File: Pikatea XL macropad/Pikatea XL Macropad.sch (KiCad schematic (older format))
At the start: 40 parts, among them J1 TC2030-CTX, J2 USB_B_Mini, J3 Conn_01x03_Male, J7 Conn_01x03_Male, SW1 SW_DPST, SW2 Rotary_Encoder_Switch, SW3 Rotary_Encoder_Switch, U1 ATMEGA32U4-EP, X1 16MHz

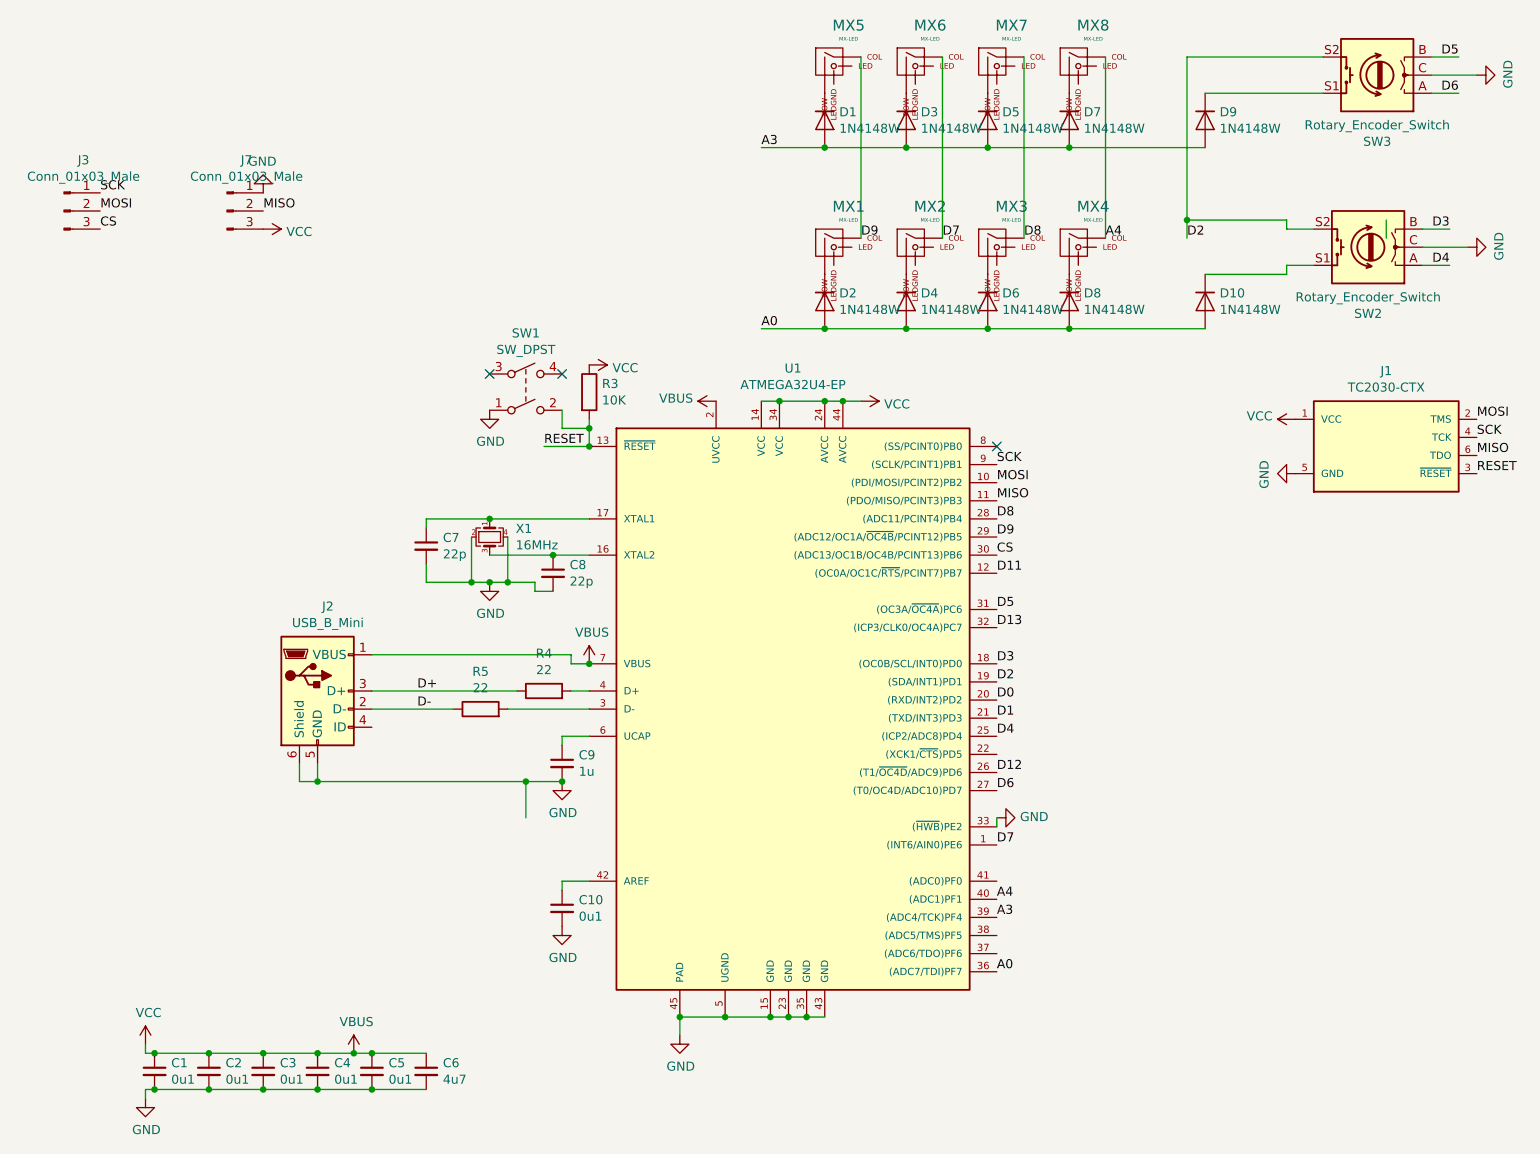
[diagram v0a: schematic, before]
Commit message: add xl macropad pcb
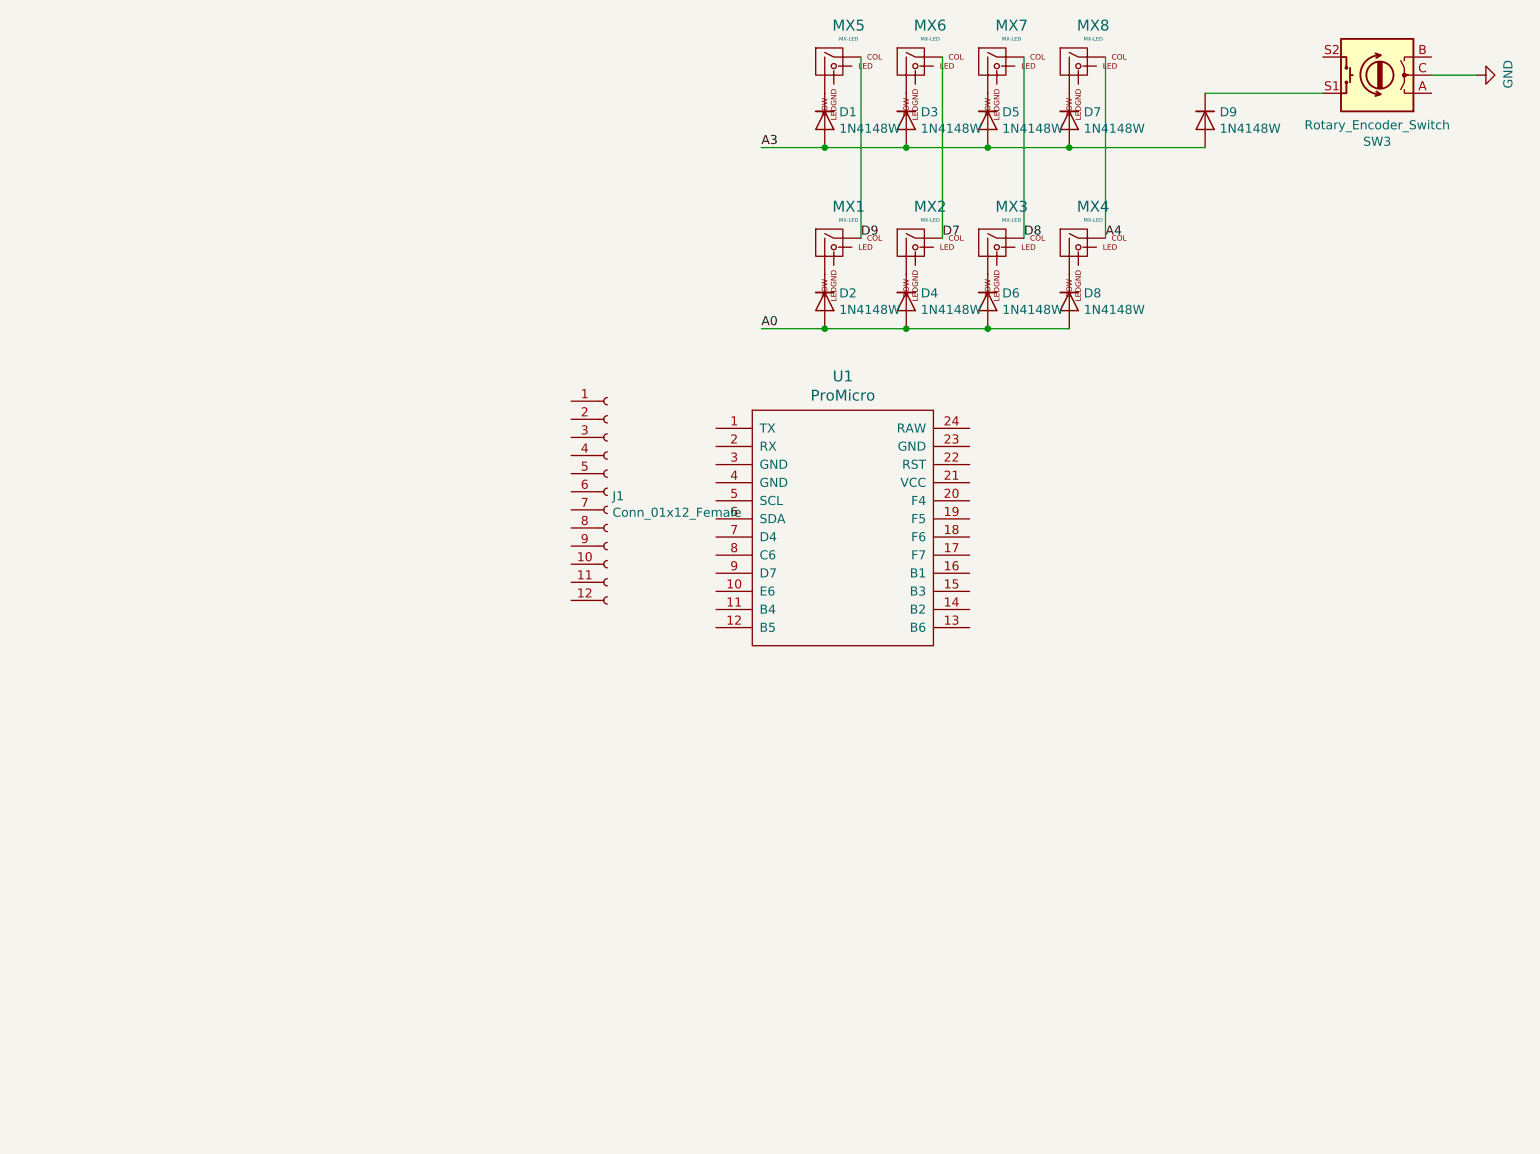
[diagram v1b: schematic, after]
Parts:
- removed C1, C10, C2, C3, C4, C5: 0u1, Capacitor_SMD:C_0805_2012Metric, symbol Device:C_Small
- removed C6: 4u7, Capacitor_SMD:C_0805_2012Metric, symbol Device:C_Small
- removed C7, C8: 22p, Capacitor_SMD:C_0805_2012Metric, symbol Device:C_Small
- removed C9: 1u, Capacitor_SMD:C_0805_2012Metric, symbol Device:C_Small
- removed D10: 1N4148W, Diode_SMD:D_SOD-123, symbol Diode:1N4148W
- removed J1: TC2030-CTX, TC2030-CTX:TC2030-IDC, symbol TC2030-CTX:TC2030-CTX
- removed J2: USB_B_Mini, usb_mini:USB-Mini-B_ LCSC-C46398, symbol Connector:USB_B_Mini
- removed J3, J7: Conn_01x03_Male, Connector_PinHeader_2.54mm:PinHeader_1x03_P2.54mm_Vertical, symbol Connector:Conn_01x03_Male
- removed R3: 10K, Resistor_SMD:R_0805_2012Metric, symbol Device:R
- removed R4, R5: 22, Resistor_SMD:R_0805_2012Metric, symbol Device:R
- removed SW1: SW_DPST, Button_Switch_SMD:SW_SPST_TL3342, symbol Switch:SW_DPST
- removed SW2: Rotary_Encoder_Switch, Pikatea Macropad Encoder Side Mount:Encoder-BI_EN11_HSM0E, symbol Device:Rotary_Encoder_Switch
- removed U1: ATMEGA32U4-EP, Package_QFP:LQFP-44_10x10mm_P0.8mm, symbol atmega32u4-ep:ATMEGA32U4-EP
- removed X1: 16MHz, Crystal:Crystal_SMD_SeikoEpson_FA238-4Pin_3.2x2.5mm, symbol Device:Crystal_GND24_Small
- added J1: Conn_01x12_Female, Connector_PinHeader_2.54mm:PinHeader_1x12_P2.54mm_Vertical, symbol Connector:Conn_01x12_Female
- added U1: ProMicro, promicro:ProMicro, symbol promicro:ProMicro
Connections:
- net labels removed: CS, D+, D-, D0, D1, D11, D12, D13, D2, D3, D4, D5, D6, MISO, MOSI, RESET, SCK, VBUS, VCC
- wire segments 93 -> 15
- no-connect marks 3 -> 0

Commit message: updates to XL macropad
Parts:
- D1, D2, D3, D4, D5, D6, D7, D8, D9: footprint Diode_SMD:D_SOD-123 -> keyboard_parts:D_axial
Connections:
- net A0: now also J1.11 (Pin_11), U1.11 (B4)
- net A3: now also J1.10 (Pin_10), U1.10 (E6)
- net A4: now also J1.12 (Pin_12), U1.12 (B5)
- net D7: now also J1.8 (Pin_8), U1.8 (C6)
- net D9: now also J1.9 (Pin_9), U1.9 (D7)
- net GND: now also J1.3 (Pin_3), J1.4 (Pin_4), U1.3 (GND), U1.4 (GND)
- net A: now reaches SW3.A
- net A: now also J1.7 (Pin_7), U1.7 (D4)
- net B: now reaches SW3.B
- net B: now also J1.6 (Pin_6), U1.6 (SDA)
- net A10: now reaches SW3.S2
- net A10: now also J1.1 (Pin_1), U1.1 (TX)
- net at J1.2 (Pin_2): now also U1.2 (RX)
- net at J1.5 (Pin_5): now also U1.5 (SCL)
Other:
- moved on the sheet: J1
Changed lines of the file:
@@
 F 0 "D1" V 7204 1330 50  0000 L CNN
 F 1 "1N4148W" V 7295 1330 50  0000 L CNN
-F 2 "Diode_SMD:D_SOD-123" H 7250 1075 50  0001 C CNN
+F 2 "keyboard_parts:D_axial" H 7250 1075 50  0001 C CNN
 F 3 "https://www.vishay.com/docs/85748/1n4148w.pdf" H 7250 1250 50  0001 C CNN
 	1    7250 1250
@@
 F 0 "D3" V 7654 1330 50  0000 L CNN
 F 1 "1N4148W" V 7745 1330 50  0000 L CNN
-F 2 "Diode_SMD:D_SOD-123" H 7700 1075 50  0001 C CNN
+F 2 "keyboard_parts:D_axial" H 7700 1075 50  0001 C CNN
 F 3 "https://www.vishay.com/docs/85748/1n4148w.pdf" H 7700 1250 50  0001 C CNN
 	1    7700 1250
@@
 F 0 "D5" V 8104 1330 50  0000 L CNN
 F 1 "1N4148W" V 8195 1330 50  0000 L CNN
-F 2 "Diode_SMD:D_SOD-123" H 8150 1075 50  0001 C CNN
+F 2 "keyboard_parts:D_axial" H 8150 1075 50  0001 C CNN
 F 3 "https://www.vishay.com/docs/85748/1n4148w.pdf" H 8150 1250 50  0001 C CNN
 	1    8150 1250
@@
 F 0 "D7" V 8554 1330 50  0000 L CNN
 F 1 "1N4148W" V 8645 1330 50  0000 L CNN
-F 2 "Diode_SMD:D_SOD-123" H 8600 1075 50  0001 C CNN
+F 2 "keyboard_parts:D_axial" H 8600 1075 50  0001 C CNN
 F 3 "https://www.vishay.com/docs/85748/1n4148w.pdf" H 8600 1250 50  0001 C CNN
 	1    8600 1250
@@
 F 0 "D9" V 9304 1330 50  0000 L CNN
 F 1 "1N4148W" V 9395 1330 50  0000 L CNN
-F 2 "Diode_SMD:D_SOD-123" H 9350 1075 50  0001 C CNN
+F 2 "keyboard_parts:D_axial" H 9350 1075 50  0001 C CNN
 F 3 "https://www.vishay.com/docs/85748/1n4148w.pdf" H 9350 1250 50  0001 C CNN
 	1    9350 1250
@@
 F 0 "D2" V 7204 2330 50  0000 L CNN
 F 1 "1N4148W" V 7295 2330 50  0000 L CNN
-F 2 "Diode_SMD:D_SOD-123" H 7250 2075 50  0001 C CNN
+F 2 "keyboard_parts:D_axial" H 7250 2075 50  0001 C CNN
 F 3 "https://www.vishay.com/docs/85748/1n4148w.pdf" H 7250 2250 50  0001 C CNN
 	1    7250 2250
@@
 F 0 "D4" V 7654 2330 50  0000 L CNN
 F 1 "1N4148W" V 7745 2330 50  0000 L CNN
-F 2 "Diode_SMD:D_SOD-123" H 7700 2075 50  0001 C CNN
+F 2 "keyboard_parts:D_axial" H 7700 2075 50  0001 C CNN
 F 3 "https://www.vishay.com/docs/85748/1n4148w.pdf" H 7700 2250 50  0001 C CNN
 	1    7700 2250
@@
 F 0 "D6" V 8104 2330 50  0000 L CNN
 F 1 "1N4148W" V 8195 2330 50  0000 L CNN
-F 2 "Diode_SMD:D_SOD-123" H 8150 2075 50  0001 C CNN
+F 2 "keyboard_parts:D_axial" H 8150 2075 50  0001 C CNN
 F 3 "https://www.vishay.com/docs/85748/1n4148w.pdf" H 8150 2250 50  0001 C CNN
 	1    8150 2250
@@
 F 0 "D8" V 8554 2330 50  0000 L CNN
 F 1 "1N4148W" V 8645 2330 50  0000 L CNN
-F 2 "Diode_SMD:D_SOD-123" H 8600 2075 50  0001 C CNN
+F 2 "keyboard_parts:D_axial" H 8600 2075 50  0001 C CNN
 F 3 "https://www.vishay.com/docs/85748/1n4148w.pdf" H 8600 2250 50  0001 C CNN
 	1    8600 2250
@@
 L Connector:Conn_01x12_Female J1
 U 1 1 61C5A4E4
-P 6050 3300
-F 0 "J1" H 6078 3276 50  0000 L CNN
-F 1 "Conn_01x12_Female" H 6078 3185 50  0000 L CNN
-F 2 "Connector_PinHeader_2.54mm:PinHeader_1x12_P2.54mm_Vertical" H 6050 3300 50  0001 C CNN
-F 3 "~" H 6050 3300 50  0001 C CNN
-	1    6050 3300
+P 6850 3450
+F 0 "J1" H 6878 3426 50  0000 L CNN
+F 1 "Conn_01x12_Female" H 6878 3335 50  0000 L CNN
+F 2 "Connector_PinHeader_2.54mm:PinHeader_1x12_P2.54mm_Vertical" H 6850 3450 50  0001 C CNN
+F 3 "~" H 6850 3450 50  0001 C CNN
+	1    6850 3450
 	1    0    0    -1
 $EndComp
@@
 	1    0    0    -1
 $EndComp
+Text Label 6650 4050 2    50   ~ 0
+A4
+Text Label 6650 3950 2    50   ~ 0
+A0
+Text Label 6650 3850 2    50   ~ 0
+A3
+Text Label 6650 3750 2    50   ~ 0
+D9
+Text Label 6650 3650 2    50   ~ 0
+D7
+Text Label 6650 3550 2    50   ~ 0
+A
+Text Label 6650 3450 2    50   ~ 0
+B
+Text Label 10600 1100 0    50   ~ 0
+A
+Text Label 10600 900  0    50   ~ 0
+B
+Text Label 10000 900  2    50   ~ 0
+A10
+Text Label 6650 2950 2    50   ~ 0
+A10
+$Comp
+L power:GND #PWR?
+U 1 1 61DC9E71
+P 6650 3250
+F 0 "#PWR?" H 6650 3000 50  0001 C CNN
+F 1 "GND" V 6655 3122 50  0000 R CNN
+F 2 "" H 6650 3250 50  0001 C CNN
+F 3 "" H 6650 3250 50  0001 C CNN
+	1    6650 3250
+	0    1    1    0
+$EndComp
+Connection ~ 6650 3250
+$Comp
+L power:GND #PWR?
+U 1 1 61DCA30D
+P 6650 3150
+F 0 "#PWR?" H 6650 2900 50  0001 C CNN
+F 1 "GND" V 6655 3022 50  0000 R CNN
+F 2 "" H 6650 3150 50  0001 C CNN
+F 3 "" H 6650 3150 50  0001 C CNN
+	1    6650 3150
+	0    1    1    0
+$EndComp
+Connection ~ 6650 3150
 $EndSCHEMATC

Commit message: update XL
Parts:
- MX1, MX2, MX3, MX4, MX5, MX6, MX7, MX8: footprint MX_Only:MXOnly-1U -> MX_Only:MXOnly-1U-NoLED
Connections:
- net D8: now also J1.5 (Pin_5), U1.5 (SCL)
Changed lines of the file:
@@
 F 0 "MX4" H 8732 2174 60  0000 C CNN
 F 1 "MX-LED" H 8732 2100 20  0000 C CNN
-F 2 "MX_Only:MXOnly-1U" H 8025 1925 60  0001 C CNN
+F 2 "MX_Only:MXOnly-1U-NoLED" H 8025 1925 60  0001 C CNN
 F 3 "" H 8025 1925 60  0001 C CNN
 	1    8650 1950
@@
 F 0 "MX3" H 8282 2174 60  0000 C CNN
 F 1 "MX-LED" H 8282 2100 20  0000 C CNN
-F 2 "MX_Only:MXOnly-1U" H 7575 1925 60  0001 C CNN
+F 2 "MX_Only:MXOnly-1U-NoLED" H 7575 1925 60  0001 C CNN
 F 3 "" H 7575 1925 60  0001 C CNN
 	1    8200 1950
@@
 F 0 "MX5" H 7382 1174 60  0000 C CNN
 F 1 "MX-LED" H 7382 1100 20  0000 C CNN
-F 2 "MX_Only:MXOnly-1U" H 6675 925 60  0001 C CNN
+F 2 "MX_Only:MXOnly-1U-NoLED" H 6675 925 60  0001 C CNN
 F 3 "" H 6675 925 60  0001 C CNN
 	1    7300 950
@@
 F 0 "MX6" H 7832 1174 60  0000 C CNN
 F 1 "MX-LED" H 7832 1100 20  0000 C CNN
-F 2 "MX_Only:MXOnly-1U" H 7125 925 60  0001 C CNN
+F 2 "MX_Only:MXOnly-1U-NoLED" H 7125 925 60  0001 C CNN
 F 3 "" H 7125 925 60  0001 C CNN
 	1    7750 950
@@
 F 0 "MX1" H 7382 2174 60  0000 C CNN
 F 1 "MX-LED" H 7382 2100 20  0000 C CNN
-F 2 "MX_Only:MXOnly-1U" H 6675 1925 60  0001 C CNN
+F 2 "MX_Only:MXOnly-1U-NoLED" H 6675 1925 60  0001 C CNN
 F 3 "" H 6675 1925 60  0001 C CNN
 	1    7300 1950
@@
 F 0 "MX2" H 7832 2174 60  0000 C CNN
 F 1 "MX-LED" H 7832 2100 20  0000 C CNN
-F 2 "MX_Only:MXOnly-1U" H 7125 1925 60  0001 C CNN
+F 2 "MX_Only:MXOnly-1U-NoLED" H 7125 1925 60  0001 C CNN
 F 3 "" H 7125 1925 60  0001 C CNN
 	1    7750 1950
@@
 F 0 "MX8" H 8732 1174 60  0000 C CNN
 F 1 "MX-LED" H 8732 1100 20  0000 C CNN
-F 2 "MX_Only:MXOnly-1U" H 8025 925 60  0001 C CNN
+F 2 "MX_Only:MXOnly-1U-NoLED" H 8025 925 60  0001 C CNN
 F 3 "" H 8025 925 60  0001 C CNN
 	1    8650 950
@@
 F 0 "MX7" H 8282 1174 60  0000 C CNN
 F 1 "MX-LED" H 8282 1100 20  0000 C CNN
-F 2 "MX_Only:MXOnly-1U" H 7575 925 60  0001 C CNN
+F 2 "MX_Only:MXOnly-1U-NoLED" H 7575 925 60  0001 C CNN
 F 3 "" H 7575 925 60  0001 C CNN
 	1    8200 950
@@
 Text Label 10000 900  2    50   ~ 0
 A10
-Text Label 6650 2950 2    50   ~ 0
-A10
-$Comp
-L power:GND #PWR?
+$Comp
+L power:GND #PWR0102
 U 1 1 61DC9E71
 P 6650 3250
-F 0 "#PWR?" H 6650 3000 50  0001 C CNN
+F 0 "#PWR0102" H 6650 3000 50  0001 C CNN
 F 1 "GND" V 6655 3122 50  0000 R CNN
 F 2 "" H 6650 3250 50  0001 C CNN
@@
 Connection ~ 6650 3250
 $Comp
-L power:GND #PWR?
+L power:GND #PWR0103
 U 1 1 61DCA30D
 P 6650 3150
-F 0 "#PWR?" H 6650 2900 50  0001 C CNN
+F 0 "#PWR0103" H 6650 2900 50  0001 C CNN
 F 1 "GND" V 6655 3022 50  0000 R CNN
 F 2 "" H 6650 3150 50  0001 C CNN
@@
 $EndComp
 Connection ~ 6650 3150
+Text Label 6650 3350 2    50   ~ 0
+D8
+Text Label 6650 2950 2    50   ~ 0
+A10
 $EndSCHEMATC
